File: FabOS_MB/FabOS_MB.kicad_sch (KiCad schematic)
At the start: 2 parts, among them U1 STM32F407VETx

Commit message: MàJ Kicad
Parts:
- OmronElectronicsG6BK-1114P-US-DC3: LCSC (none) -> C1563013; MPN (none) -> G6BK-1114P-US-DC3
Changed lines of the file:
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@@
 		(on_board yes)
 		(dnp no)
-		(fields_autoplaced yes)
 		(property "Reference" "OmronElectronicsG6BK-1114P-US-DC3"
 			(at 129.54 43.18 0)
@@
 			)
 		)
-		(property "Datasheet" ""
+		(property "Datasheet" "https://www.lcsc.com/datasheet/lcsc_datasheet_2211282100_Omron-Electronics-G6BK-1114P-US-DC3_C1563013.pdf"
 			(at 107.95 33.02 0)
 			(effects
@@
 			)
 		)
-		(property "Description" ""
-			(at 107.95 33.02 0)
+		(property "Description" "Relais bistable"
+			(at 141.732 37.846 0)
+			(effects
+				(font
+					(size 1.27 1.27)
+				)
+			)
+		)
+		(property "MPN" " G6BK-1114P-US-DC3"
+			(at 128.27 33.02 0)
+			(effects
+				(font
+					(size 1.27 1.27)
+				)
+				(hide yes)
+			)
+		)
+		(property "LCSC" " C1563013"
+			(at 128.27 33.02 0)
 			(effects
 				(font
@@
 		(pin "6"
 		)
+		(pin "5"
+		)
+		(pin "2"
+		)
 		(instances

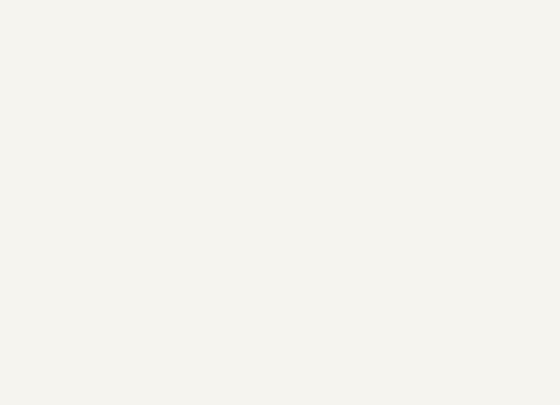
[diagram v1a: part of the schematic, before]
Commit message: Symbole + empreinte Transformateur
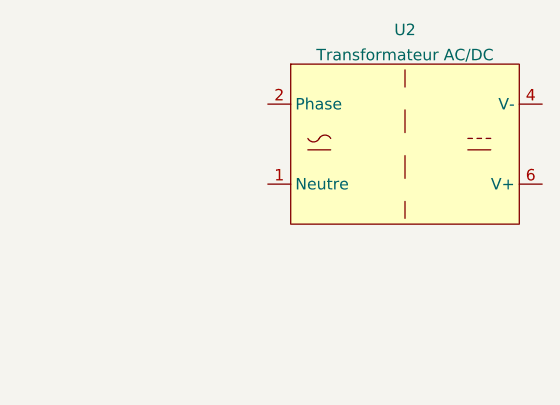
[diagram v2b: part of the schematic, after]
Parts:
- added U2: ~, Librairie_MB:TD POWER TAS12-5-W2, symbol Librairie_MB:Transformateur
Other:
- company: (none) -> ENSEA
- title: (none) -> Carte mère FabOS
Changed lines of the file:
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@@
 	(generator_version "8.0")
 	(paper "A4")
+	(title_block
+		(title "Carte mère FabOS")
+		(rev "1.0.0")
+		(company "ENSEA")
+	)
 	(symbol
 		(lib_id "MCU_ST_STM32F4:STM32F407VETx")
@@
 					(unit 1)
 				)
+			)
+		)
+	)
+	(symbol
+		(lib_id "Librairie_MB:Transformateur")
+		(at 205.74 35.56 0)
+		(unit 1)
+		(exclude_from_sim no)
+		(in_bom yes)
+		(on_board yes)
+		(dnp no)
+		(property "Reference" "U2"
+			(at 205.74 22.86 0)
+			(effects
+				(font
+					(size 1.27 1.27)
+				)
+			)
+		)
+		(property "Value" "~"
+			(at 205.74 25.4 0)
+			(effects
+				(font
+					(size 1.27 1.27)
+				)
+			)
+		)
+		(property "Footprint" "Librairie_MB:TD POWER TAS12-5-W2"
+			(at 205.74 35.56 0)
+			(effects
+				(font
+					(size 1.27 1.27)
+				)
+				(hide yes)
+			)
+		)
+		(property "Datasheet" "https://www.lcsc.com/datasheet/lcsc_datasheet_2307141637_TDPOWER-TAS12-5-W2_C5354760.pdf"
+			(at 205.74 35.56 0)
+			(effects
+				(font
+					(size 1.27 1.27)
+				)
+				(hide yes)
+			)
+		)
+		(property "Description" "Transformateur AC/DC"
+			(at 205.74 25.654 0)
+			(effects
+				(font
+					(size 1.27 1.27)
+				)
+			)
+		)
+		(property "MPN" " TAS12-5-W2"
+			(at 205.74 35.56 0)
+			(effects
+				(font
+					(size 1.27 1.27)
+				)
+				(hide yes)
+			)
+		)
+		(property "LCSC" " C5354760"
+			(at 205.74 35.56 0)
+			(effects
+				(font
+					(size 1.27 1.27)
+				)
+				(hide yes)
+			)
+		)
+		(pin "1"
+		)
+		(pin "2"
+		)
+		(pin "4"
+		)
+		(pin "6"
+		)
+		(instances
+			(project ""
+				(path "/09377d5d-727f-4ff4-92c8-7a0483d23f1e"
+					(reference "U2")
+					(unit 1)
+				)

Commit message: Mise à jour empreintes
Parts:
- added J1: USB_A, Librairie_MB:USB_A_Femelle, symbol Connector:USB_A
- added U3: ~, Librairie_MB:Regulateur_tension_5V_3V3, symbol Librairie_MB:Regulateur_tension
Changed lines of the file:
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@@
+		)
+	)
+	(symbol
+		(lib_id "Connector:USB_A")
+		(at 255.27 38.1 0)
+		(unit 1)
+		(exclude_from_sim no)
+		(in_bom yes)
+		(on_board yes)
+		(dnp no)
+		(fields_autoplaced yes)
+		(property "Reference" "J1"
+			(at 255.27 25.4 0)
+			(effects
+				(font
+					(size 1.27 1.27)
+				)
+			)
+		)
+		(property "Value" "USB_A"
+			(at 255.27 27.94 0)
+			(effects
+				(font
+					(size 1.27 1.27)
+				)
+			)
+		)
+		(property "Footprint" "Librairie_MB:USB_A_Femelle"
+			(at 259.08 39.37 0)
+			(effects
+				(font
+					(size 1.27 1.27)
+				)
+				(hide yes)
+			)
+		)
+		(property "Datasheet" "https://www.lcsc.com/datasheet/lcsc_datasheet_2103011233_Jing-Extension-of-the-Electronic-Co--908-371A1011D10100_C42576.pdf"
+			(at 259.08 39.37 0)
+			(effects
+				(font
+					(size 1.27 1.27)
+				)
+				(hide yes)
+			)
+		)
+		(property "Description" "USB Type A connector"
+			(at 255.27 38.1 0)
+			(effects
+				(font
+					(size 1.27 1.27)
+				)
+				(hide yes)
+			)
+		)
+		(property "MPN" "  908-371A1011D10100"
+			(at 255.27 38.1 0)
+			(effects
+				(font
+					(size 1.27 1.27)
+				)
+				(hide yes)
+			)
+		)
+		(property "LCSC" "  C42576"
+			(at 255.27 38.1 0)
+			(effects
+				(font
+					(size 1.27 1.27)
+				)
+				(hide yes)
+			)
+		)
+		(pin "2"
+		)
+		(pin "4"
+		)
+		(pin "1"
+		)
+		(pin "3"
+		)
+		(instances
+			(project ""
+				(path "/09377d5d-727f-4ff4-92c8-7a0483d23f1e"
+					(reference "J1")
+					(unit 1)
+				)
+			)
+		)
+	)
+	(symbol
+		(lib_id "Librairie_MB:Regulateur_tension")
+		(at 204.47 71.12 0)
+		(unit 1)
+		(exclude_from_sim no)
+		(in_bom yes)
+		(on_board yes)
+		(dnp no)
+		(fields_autoplaced yes)
+		(property "Reference" "U3"
+			(at 204.7875 60.96 0)
+			(effects
+				(font
+					(size 1.27 1.27)
+				)
+			)
+		)
+		(property "Value" "~"
+			(at 204.7875 63.5 0)
+			(effects
+				(font
+					(size 1.27 1.27)
+				)
+			)
+		)
+		(property "Footprint" "Librairie_MB:Regulateur_tension_5V_3V3"
+			(at 203.835 81.28 0)
+			(effects
+				(font
+					(size 1.27 1.27)
+				)
+				(hide yes)
+			)
+		)
+		(property "Datasheet" "https://www.lcsc.com/datasheet/lcsc_datasheet_2304140030_Seaward-Elec-SE5218ALG-LF_C118233.pdf"
+			(at 207.645 53.34 0)
+			(effects
+				(font
+					(size 1.27 1.27)
+				)
+				(hide yes)
+			)
+		)
+		(property "Description" ""
+			(at 204.47 71.12 0)
+			(effects
+				(font
+					(size 1.27 1.27)
+				)
+				(hide yes)
+			)
+		)
+		(property "MPN" "  SE5218ALG-LF"
+			(at 204.47 56.515 0)
+			(effects
+				(font
+					(size 1.27 1.27)
+				)
+				(hide yes)
+			)
+		)
+		(property "LCSC" "C118233"
+			(at 205.74 59.055 0)
+			(effects
+				(font
+					(size 1.27 1.27)
+				)
+				(hide yes)
+			)
+		)
+		(pin "4"
+		)
+		(pin "1"
+		)
+		(pin "2"
+		)
+		(pin "3"
+		)
+		(pin "5"
+		)
+		(instances
+			(project ""
+				(path "/09377d5d-727f-4ff4-92c8-7a0483d23f1e"
+					(reference "U3")
+					(unit 1)
+				)
+			)
 		)
 	)

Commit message: Ajout empreinte USB-C
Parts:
- added J2: USB_C_Receptacle, Librairie_MB:USB_C_femelle_12P, symbol Connector:USB_C_Receptacle
- added U4: USBLC6-2SC6, Package_TO_SOT_SMD:SOT-23-6, symbol Power_Protection:USBLC6-2SC6
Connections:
- new net: J2.A1 (GND), J2.A12 (GND), J2.B1 (GND), J2.B12 (GND)
- new net: J2.A4 (VBUS), J2.A9 (VBUS), J2.B4 (VBUS), J2.B9 (VBUS)
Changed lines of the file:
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@@
+	)
+	(symbol
+		(lib_id "Connector:USB_C_Receptacle")
+		(at 250.19 97.79 0)
+		(unit 1)
+		(exclude_from_sim no)
+		(in_bom yes)
+		(on_board yes)
+		(dnp no)
+		(fields_autoplaced yes)
+		(property "Reference" "J2"
+			(at 250.19 64.77 0)
+			(effects
+				(font
+					(size 1.27 1.27)
+				)
+			)
+		)
+		(property "Value" "USB_C_Receptacle"
+			(at 250.19 67.31 0)
+			(effects
+				(font
+					(size 1.27 1.27)
+				)
+			)
+		)
+		(property "Footprint" "Librairie_MB:USB_C_femelle_12P"
+			(at 254 97.79 0)
+			(effects
+				(font
+					(size 1.27 1.27)
+				)
+				(hide yes)
+			)
+		)
+		(property "Datasheet" "https://www.lcsc.com/datasheet/lcsc_datasheet_2009111836_SOFNG-MC-311D_C136423.pdf"
+			(at 254 97.79 0)
+			(effects
+				(font
+					(size 1.27 1.27)
+				)
+				(hide yes)
+			)
+		)
+		(property "Description" "USB 12P"
+			(at 250.19 97.79 0)
+			(effects
+				(font
+					(size 1.27 1.27)
+				)
+				(hide yes)
+			)
+		)
+		(property "MPN" "MC-311D"
+			(at 250.19 97.79 0)
+			(effects
+				(font
+					(size 1.27 1.27)
+				)
+				(hide yes)
+			)
+		)
+		(property "LCSC" "C136423"
+			(at 250.19 97.79 0)
+			(effects
+				(font
+					(size 1.27 1.27)
+				)
+				(hide yes)
+			)
+		)
+		(pin "S1"
+		)
+		(pin "A5"
+		)
+		(pin "A7"
+		)
+		(pin "B7"
+		)
+		(pin "B5"
+		)
+		(pin "A12"
+		)
+		(pin "A6"
+		)
+		(pin "A9"
+		)
+		(pin "A4"
+		)
+		(pin "B8"
+		)
+		(pin "A8"
+		)
+		(pin "B1"
+		)
+		(pin "B6"
+		)
+		(pin "B12"
+		)
+		(pin "B4"
+		)
+		(pin "B9"
+		)
+		(pin "A1"
+		)
+		(instances
+			(project ""
+				(path "/09377d5d-727f-4ff4-92c8-7a0483d23f1e"
+					(reference "J2")
+					(unit 1)
+				)
+			)
+		)
+	)
+	(symbol
+		(lib_id "Power_Protection:USBLC6-2SC6")
+		(at 209.55 95.25 0)
+		(unit 1)
+		(exclude_from_sim no)
+		(in_bom yes)
+		(on_board yes)
+		(dnp no)
+		(fields_autoplaced yes)
+		(property "Reference" "U4"
+			(at 211.2011 87.63 0)
+			(effects
+				(font
+					(size 1.27 1.27)
+				)
+				(justify left)
+			)
+		)
+		(property "Value" "USBLC6-2SC6"
+			(at 211.2011 90.17 0)
+			(effects
+				(font
+					(size 1.27 1.27)
+				)
+				(justify left)
+			)
+		)
+		(property "Footprint" "Package_TO_SOT_SMD:SOT-23-6"
+			(at 210.82 101.6 0)
+			(effects
+				(font
+					(size 1.27 1.27)
+					(italic yes)
+				)
+				(justify left)
+				(hide yes)
+			)
+		)
+		(property "Datasheet" "https://www.st.com/resource/en/datasheet/usblc6-2.pdf"
+			(at 210.82 103.505 0)
+			(effects
+				(font
+					(size 1.27 1.27)
+				)
+				(justify left)
+				(hide yes)
+			)
+		)
+		(property "Description" "Very low capacitance ESD protection diode, 2 data-line, SOT-23-6"
+			(at 209.55 95.25 0)
+			(effects
+				(font
+					(size 1.27 1.27)
+				)
+				(hide yes)
+			)
+		)
+		(pin "2"
+		)
+		(pin "1"
+		)
+		(pin "4"
+		)
+		(pin "5"
+		)
+		(pin "6"
+		)
+		(pin "3"
+		)
+		(instances
+			(project ""
+				(path "/09377d5d-727f-4ff4-92c8-7a0483d23f1e"
+					(reference "U4")
+					(unit 1)
+				)
+			)
+		)
 	)
 	(symbol

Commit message: Empreintes
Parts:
- removed OmronElectronicsG6BK-1114P-US-DC3: ~, Librairie_MB:Omron Electronics G6BK-1114P-US-DC3, symbol Librairie_MB:Omron_Electronics_G6BK-1114P-US-DC3
- added J3: RJ45, Librairie_MB:RJ_45_Chinois, symbol Connector:RJ45
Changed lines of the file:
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@@
+	)
+	(symbol
+		(lib_id "Connector:RJ45")
+		(at 208.28 128.27 0)
+		(unit 1)
+		(exclude_from_sim no)
+		(in_bom yes)
+		(on_board yes)
+		(dnp no)
+		(fields_autoplaced yes)
+		(property "Reference" "J3"
+			(at 208.28 110.49 0)
+			(effects
+				(font
+					(size 1.27 1.27)
+				)
+			)
+		)
+		(property "Value" "RJ45"
+			(at 208.28 113.03 0)
+			(effects
+				(font
+					(size 1.27 1.27)
+				)
+			)
+		)
+		(property "Footprint" "Librairie_MB:RJ_45_Chinois"
+			(at 208.28 127.635 90)
+			(effects
+				(font
+					(size 1.27 1.27)
+				)
+				(hide yes)
+			)
+		)
+		(property "Datasheet" "https://www.lcsc.com/datasheet/lcsc_datasheet_2009081108_RCH-RC00417_C708605.pdf"
+			(at 208.28 127.635 90)
+			(effects
+				(font
+					(size 1.27 1.27)
+				)
+				(hide yes)
+			)
+		)
+		(property "Description" "RJ connector, 8P8C (8 positions 8 connected)"
+			(at 208.28 128.27 0)
+			(show_name yes)
+			(effects
+				(font
+					(size 1.27 1.27)
+				)
+				(hide yes)
+			)
+		)
+		(pin "8"
+		)
+		(pin "6"
+		)
+		(pin "7"
+		)
+		(pin "4"
+		)
+		(pin "5"
+		)
+		(pin "2"
+		)
+		(pin "3"
+		)
+		(pin "1"
+		)
+		(instances
+			(project ""
+				(path "/09377d5d-727f-4ff4-92c8-7a0483d23f1e"
+					(reference "J3")
+					(unit 1)
+				)
+			)
+		)
 	)
 	(symbol
@@
 					(unit 1)
 				)
-			)
-		)
-	)
-	(symbol
-		(lib_id "Librairie_MB:Omron_Electronics_G6BK-1114P-US-DC3")
-		(at 128.27 33.02 0)
-		(unit 1)
-		(exclude_from_sim no)
-		(in_bom yes)
-		(on_board yes)
-		(dnp no)
-		(property "Reference" "OmronElectronicsG6BK-1114P-US-DC3"
-			(at 129.54 43.18 0)
-			(effects
-				(font
-					(size 1.27 1.27)
-				)
-			)
-		)
-		(property "Value" "~"
-			(at 107.95 33.02 0)
-			(effects
-				(font
-					(size 1.27 1.27)
-				)
-			)
-		)
-		(property "Footprint" "Librairie_MB:Omron Electronics G6BK-1114P-US-DC3"
-			(at 129.54 44.45 0)
-			(effects
-				(font
-					(size 1.27 1.27)
-				)
-				(hide yes)
-			)
-		)
-		(property "Datasheet" "https://www.lcsc.com/datasheet/lcsc_datasheet_2211282100_Omron-Electronics-G6BK-1114P-US-DC3_C1563013.pdf"
-			(at 107.95 33.02 0)
-			(effects
-				(font
-					(size 1.27 1.27)
-				)
-				(hide yes)
-			)
-		)
-		(property "Description" "Relais bistable"
-			(at 141.732 37.846 0)
-			(effects
-				(font
-					(size 1.27 1.27)
-				)
-			)
-		)
-		(property "MPN" " G6BK-1114P-US-DC3"
-			(at 128.27 33.02 0)
-			(effects
-				(font
-					(size 1.27 1.27)
-				)
-				(hide yes)
-			)
-		)
-		(property "LCSC" " C1563013"
-			(at 128.27 33.02 0)
-			(effects
-				(font
-					(size 1.27 1.27)
-				)
-				(hide yes)
-			)
-		)
-		(pin "4"
-		)
-		(pin "3"
-		)
-		(pin "1"
-		)
-		(pin "6"
-		)
-		(pin "5"
-		)
-		(pin "2"
-		)
-		(instances
-			(project ""
-				(path "/09377d5d-727f-4ff4-92c8-7a0483d23f1e"
-					(reference "OmronElectronicsG6BK-1114P-US-DC3")
-					(unit 1)
-				)

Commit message: add link
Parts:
- removed U3: ~, Librairie_MB:Regulateur_tension_5V_3V3, symbol Librairie_MB:Regulateur_tension
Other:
- note added: "A changer par un régulateur à découpage 12v -> 3v type Buck, Step-down"
- note added: "Convertisseur Flyback 230V AC / 110VV AC 50-60Hz -> 12V DC (calculer le courant nécessaire)"
- note added: "Relay 12V DC switching 230V AC / 16A"
- note added: "https://www.lcsc.com/product-detail/DC-DC-Converters_Texas-Instruments-TPS563201DDCR_C116592.html"
- note added: "https://www.lcsc.com/product-detail/LIN-Transceivers_onsemi-NCV7329D10R2G_C603984.html"
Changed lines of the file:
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@@
 		(company "ENSEA")
+	)
+	(text "Relay \n12V DC switching\n230V AC / 16A"
+		(exclude_from_sim no)
+		(at 128.016 115.824 0)
+		(effects
+			(font
+				(size 1.27 1.27)
+			)
+		)
+	)
+	(text "A changer par un régulateur à découpage 12v -> 3v type Buck, Step-down"
+		(exclude_from_sim no)
+		(at 126.238 34.29 0)
+		(effects
+			(font
+				(size 1.27 1.27)
+			)
+		)
+	)
+	(text "Convertisseur Flyback 230V AC / 110VV AC 50-60Hz -> 12V DC (calculer le courant nécessaire)"
+		(exclude_from_sim no)
+		(at 205.74 19.304 0)
+		(effects
+			(font
+				(size 1.27 1.27)
+			)
+		)
+	)
+	(text "https://www.lcsc.com/product-detail/DC-DC-Converters_Texas-Instruments-TPS563201DDCR_C116592.html"
+		(exclude_from_sim no)
+		(at 129.286 30.226 0)
+		(effects
+			(font
+				(size 1.27 1.27)
+			)
+		)
+	)
+	(text "https://www.lcsc.com/product-detail/LIN-Transceivers_onsemi-NCV7329D10R2G_C603984.html"
+		(exclude_from_sim no)
+		(at 127.508 50.8 0)
+		(effects
+			(font
+				(size 1.27 1.27)
+			)
+		)
 	)
 	(symbol
@@
 					(unit 1)
 				)
-			)
-		)
-	)
-	(symbol
-		(lib_id "Librairie_MB:Regulateur_tension")
-		(at 204.47 71.12 0)
-		(unit 1)
-		(exclude_from_sim no)
-		(in_bom yes)
-		(on_board yes)
-		(dnp no)
-		(fields_autoplaced yes)
-		(property "Reference" "U3"
-			(at 204.7875 60.96 0)
-			(effects
-				(font
-					(size 1.27 1.27)
-				)
-			)
-		)
-		(property "Value" "~"
-			(at 204.7875 63.5 0)
-			(effects
-				(font
-					(size 1.27 1.27)
-				)
-			)
-		)
-		(property "Footprint" "Librairie_MB:Regulateur_tension_5V_3V3"
-			(at 203.835 81.28 0)
-			(effects
-				(font
-					(size 1.27 1.27)
-				)
-				(hide yes)
-			)
-		)
-		(property "Datasheet" "https://www.lcsc.com/datasheet/lcsc_datasheet_2304140030_Seaward-Elec-SE5218ALG-LF_C118233.pdf"
-			(at 207.645 53.34 0)
-			(effects
-				(font
-					(size 1.27 1.27)
-				)
-				(hide yes)
-			)
-		)
-		(property "Description" ""
-			(at 204.47 71.12 0)
-			(effects
-				(font
-					(size 1.27 1.27)
-				)
-				(hide yes)
-			)
-		)
-		(property "MPN" "  SE5218ALG-LF"
-			(at 204.47 56.515 0)
-			(effects
-				(font
-					(size 1.27 1.27)
-				)
-				(hide yes)
-			)
-		)
-		(property "LCSC" "C118233"
-			(at 205.74 59.055 0)
-			(effects
-				(font
-					(size 1.27 1.27)
-				)
-				(hide yes)
-			)
-		)
-		(pin "4"
-		)
-		(pin "1"
-		)
-		(pin "2"
-		)
-		(pin "3"
-		)
-		(pin "5"
-		)
-		(instances
-			(project ""
-				(path "/09377d5d-727f-4ff4-92c8-7a0483d23f1e"
-					(reference "U3")
-					(unit 1)
-				)
